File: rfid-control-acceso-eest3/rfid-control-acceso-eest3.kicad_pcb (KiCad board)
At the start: 2 copper layers, 120 x 80 mm, 71 parts, among them J1 BOARD_12VDC_2.5A, J10 PIR_TAMPER, J11 PIR_PWR, J12 PIR_ALARM, J13 ESP32-S3-DevKitC-1_N16R8_44P, J2 BUCK?, J5 RC522_8PIN_3V3_PINOUT_PENDING, J6 REED_NC, J8 CABINET_SENSOR, J9 LOCK_12V_1.8A_21.6W, Q1 AO3400A_PRELIM, Q2 AO3400A_PRELIM

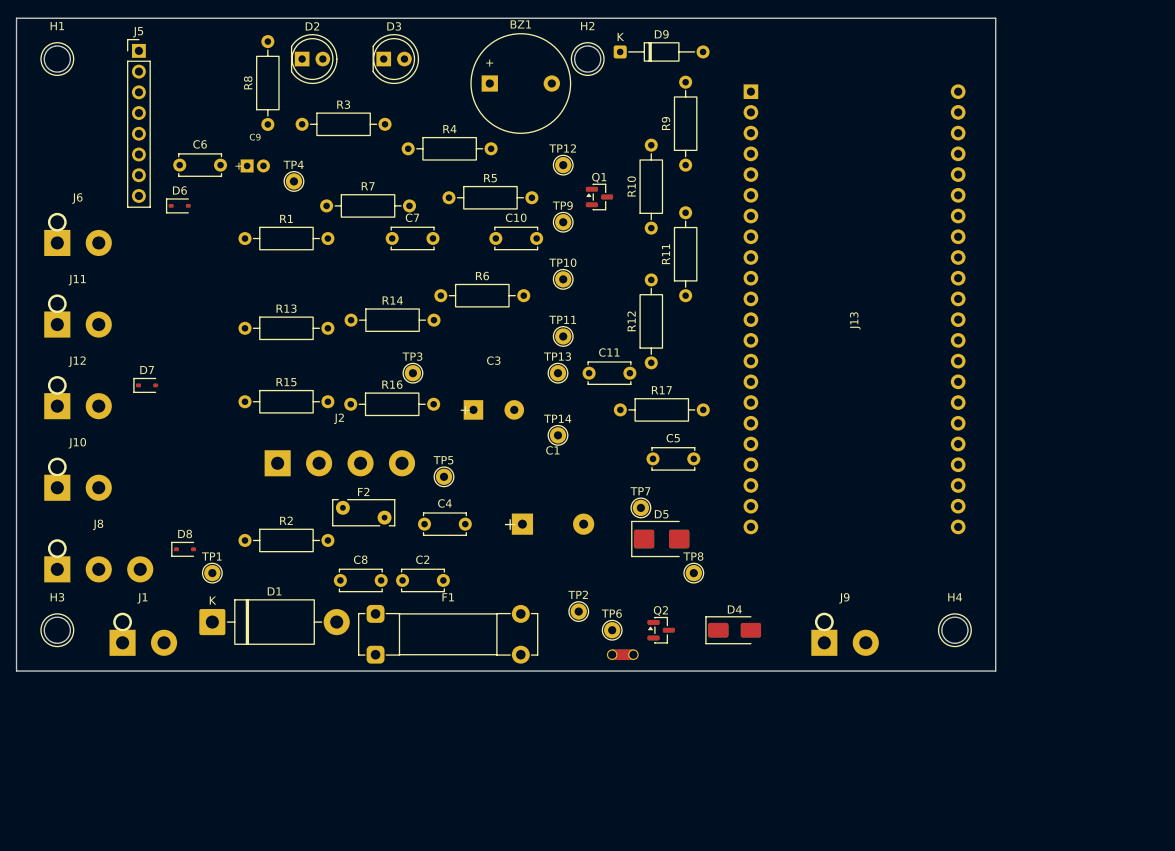
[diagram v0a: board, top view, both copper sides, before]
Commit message: Corrige tres diodos invertidos, netclasses y recalcula el floorplan
Errores electricos, verificados regenerando el netlist con kicad-cli:

- D1 tenia el catodo en +12V_IN y el anodo hacia F1, o sea bloqueaba la
  polaridad correcta. Montado asi la placa no encendia.
- D2 y D3 tenian el anodo a GND y el catodo hacia R3/R4. Como un GPIO nunca
  baja de 0 V, los LEDs no podian encender.
- La red entre D1 y F1 no coincidia con ningun patron de netclass y heredaba
  Default: 0,2 mm de pista para ~2,2 A. Pasa a LOCK_POWER (2,0 mm), igual que
  +12V_IN, que estaba en POWER_12V_AUX (0,8 mm).
- Al girar los LEDs, KiCad renombro las redes autogeneradas. Las netclasses
  apuntaban a los nombres viejos; se re-apuntaron.

Footprints: se eliminan los ocho PLACEHOLDER_NO_FABRICAR. Todos tenian
equivalente real ya instalado en KiCad 10. C9 pasa a MLCC 1206: tenia simbolo
no polarizado con footprint de electrolitico. El unico footprint local que
queda es el del ESP32-S3, con la hilera par duplicada en 22,86 y 25,40 mm
porque no se midio el modulo fisico. El paso doble cubre la separacion, no el
orden de pines: hay que verificar 3V3, EN, 5V y GND por continuidad antes de
soldar.

Floorplan: la posicion real de los pines de J13 determina el orden de los
bloques, y estaban casi invertidos. Lazo de potencia J1-J9 de 86 a 38 mm,
estrella de masa NT1-J1 de 60 a 9 mm, SPI de ~70 a 8,7 mm. Contorno de 120x80
a 140x100 mm: la densidad bajaba de 53% a 36% y la caja sigue sin definir.

Sigue sin ruteo, sin vias y sin archivos de fabricacion. Falta ejecutar
Update PCB from Schematic en la GUI: KiCad no expone esa operacion por CLI.

Co-Authored-By: Claude Opus 5 <noreply@anthropic.com>
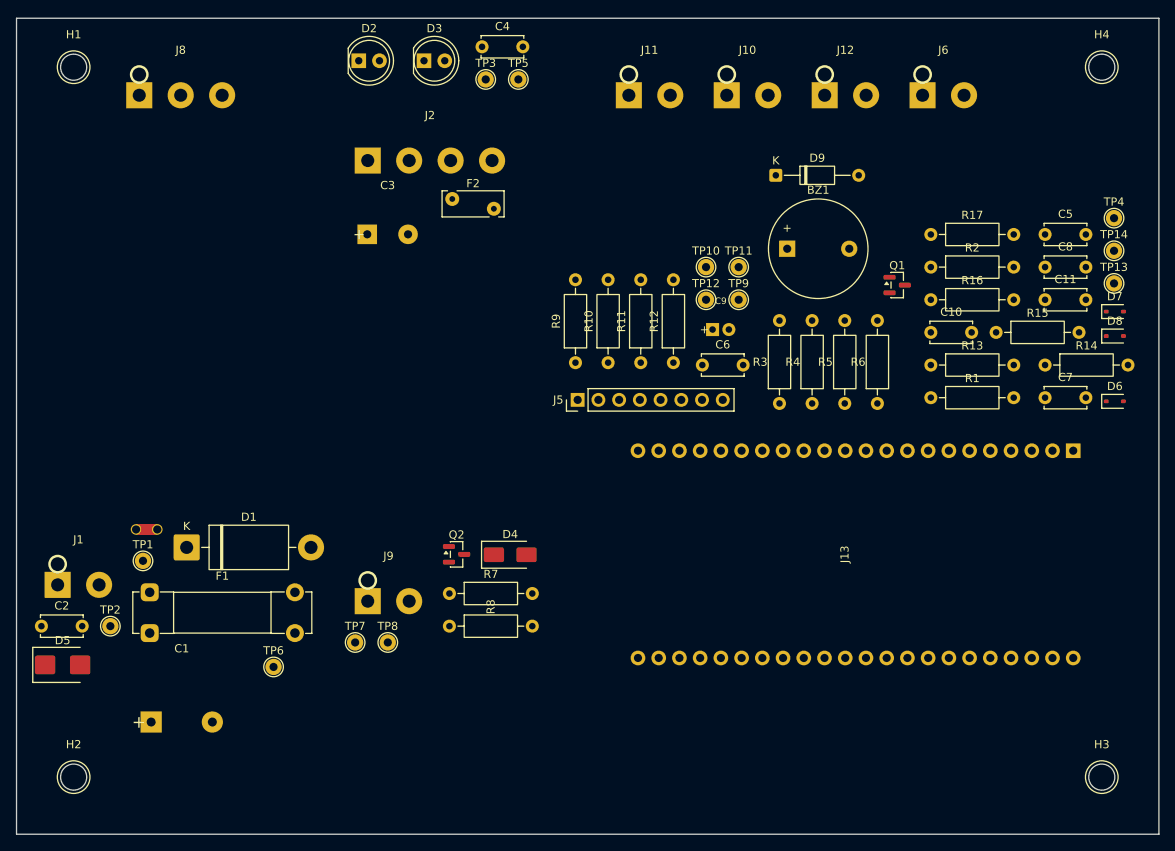
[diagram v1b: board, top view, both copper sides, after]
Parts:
- H1, H2, H3, H4: footprint rfid_eest3:MOUNTING_HOLE_3.2_PLACEHOLDER_NO_FABRICAR -> MountingHole:MountingHole_3.2mm_M3
- moved H3 129.3 mm to (153.0, 113.0)
- moved D7 118.9 mm to (154.6, 56.0)
- moved D6 117.1 mm to (154.6, 67.0)
- moved D8 116.9 mm to (154.6, 59.0)
- moved H2 108.2 mm to (27.0, 113.0)
- moved J6 107.6 mm to (131.0, 26.9)
- moved J12 101.5 mm to (119.0, 26.9)
- moved TP4 100.6 mm to (154.5, 44.5)
- moved J10 95.1 mm to (107.0, 26.9)
- moved C8 94.5 mm to (146.1, 50.5)
- moved R15 92.4 mm to (140.1, 58.5)
- moved R2 90.5 mm to (132.1, 50.5)
- moved R1 86.3 mm to (132.1, 66.5)
- moved R14 85.2 mm to (146.1, 62.5)
- moved R13 84.2 mm to (132.1, 62.5)
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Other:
- board size 120 x 80 mm -> 140 x 100 mm

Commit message: Lleva J5 al borde y le pone conector con traba para el lector del marco
El RC522 va montado en el marco de la puerta y se conecta por cable. J5 estaba
en el medio de la placa, asi que el cable tenia que cruzar por encima de todo
el board. Se mueve al borde superior, junto a las borneras de sensores: todos
los cables que van hacia la puerta salen por el mismo lado y el borde inferior
queda para potencia y cerradura.

El footprint pasa de PinHeader_1x08_P2.54mm_Vertical a JST_XH_S8B-XH-A
horizontal: con traba y entrada lateral. Un header con jumpers dupont falla de
forma intermitente en algo que golpea cada vez que se abre la puerta.

La traza SPI sube de 8,7 a 43,7 mm. Es irrelevante: con el reloj a 1 MHz y las
resistencias serie de 33 ohm, el factor dominante son los 20-40 cm de cable, no
44 mm de pista.

Como el board conserva el footprint viejo hasta que se sincronice, la
colocacion reserva la union de ambas cajas. Sin eso J5 pisaba a J2 y el DRC
reportaba cortocircuito +3V3/GND de forma transitoria.

Se documentan en el informe las condiciones de instalacion del lector:
longitud de cable, separacion del metal del marco y desacoplo local.

Co-Authored-By: Claude Opus 5 <noreply@anthropic.com>
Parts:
- moved J5 43.6 mm to (77.0, 24.8), turned to 0 degrees
- moved F2 21.3 mm to (59.4, 58.1)
- moved J2 16.1 mm to (61.0, 50.9)
- moved C3 11.2 mm to (61.0, 35.5)
- moved C4 10.0 mm to (67.0, 23.5)
- moved D2 10.0 mm to (51.9, 25.2)
- moved D3 10.0 mm to (59.9, 25.2)
- moved TP3 10.0 mm to (67.5, 27.5)
- moved TP5 10.0 mm to (71.5, 27.5)
- moved J10 9.00 mm to (116.0, 26.9)
- moved J11 9.00 mm to (104.0, 26.9)
- moved J6 9.00 mm to (140.0, 26.9)
- moved J12 9.00 mm to (128.0, 26.9)
- moved R10 5.00 mm to (92.5, 67.2)
- moved R11 5.00 mm to (96.5, 67.2)
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
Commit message: Transfiere al board los footprints reales desde el esquema
Resultado de Update PCB from Schematic en la GUI, que kicad-cli no expone.

El board pasa a tener la geometria real: J13 con los 66 pads del footprint de
doble paso (el pad 2 existe en x=22,86 y en x=25,40), J5 como JST-XH de 8 vias,
C9 como 1206 y las ocho borneras como TerminalBlock_RND. Con esto los diodos
D1, D2 y D3 quedan por fin conectados segun el esquema corregido.

DRC: 28 infracciones, todas silk_overlap. Cero de biblioteca, cero de
courtyard, cero cortocircuitos. 122 pads sin conectar, que es lo esperado
porque no hay ninguna pista.

Co-Authored-By: Claude Opus 5 <noreply@anthropic.com>
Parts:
- C1: footprint rfid_eest3:CP_Radial_D16_P7.50_PLACEHOLDER_NO_FABRICAR -> Capacitor_THT:CP_Radial_D16.0mm_P7.50mm
- C3: footprint rfid_eest3:CP_Radial_D10_P5.00_PLACEHOLDER_NO_FABRICAR -> Capacitor_THT:CP_Radial_D10.0mm_P5.00mm_P7.50mm
- C9: value 10uF_PRELIMINAR -> 10uF_X5R_16V_1206; footprint rfid_eest3:CP_Radial_D5_P2.00_PLACEHOLDER_NO_FABRICAR -> Capacitor_SMD:C_1206_3216Metric
- J1, J10, J11, J12, J6, J9: footprint rfid_eest3:KF301_2P_P5.08_PLACEHOLDER_NO_FABRICAR -> TerminalBlock_RND:TerminalBlock_RND_205-00232_1x02_P5.08mm_Horizontal
- J13: footprint rfid_eest3:ESP32-S3-DevKitC-1-44P_PLACEHOLDER_NO_FABRICAR -> rfid_eest3:ESP32-S3-44P_SOCKET_DUAL_22.86_25.40
- J2: footprint rfid_eest3:KF301_4P_P5.08_PLACEHOLDER_NO_FABRICAR -> TerminalBlock_RND:TerminalBlock_RND_205-00234_1x04_P5.08mm_Horizontal
- J5: value RC522_8PIN_3V3_PINOUT_PENDING -> RC522_8PIN_3V3_XH_CABLE_LECTOR; footprint Connector_PinHeader_2.54mm:PinHeader_1x08_P2.54mm_Vertical -> Connector_JST:JST_XH_S8B-XH-A_1x08_P2.50mm_Horizontal
- J8: footprint rfid_eest3:KF301_3P_P5.08_PLACEHOLDER_NO_FABRICAR -> TerminalBlock_RND:TerminalBlock_RND_205-00233_1x03_P5.08mm_Horizontal
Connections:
- D1 pad 1: +12V_IN -> Net-(D1-K)
- D1 pad 2: Net-(D1-A) -> +12V_IN
- D2 pad 1: Net-(D2-K) -> GND
- D2 pad 2: GND -> Net-(D2-A)
- D3 pad 1: Net-(D3-K) -> GND
- D3 pad 2: GND -> Net-(D3-A)
- F1 pad 1: Net-(D1-A) -> Net-(D1-K)
- R3 pad 2: Net-(D2-K) -> Net-(D2-A)
- R4 pad 2: Net-(D3-K) -> Net-(D3-A)

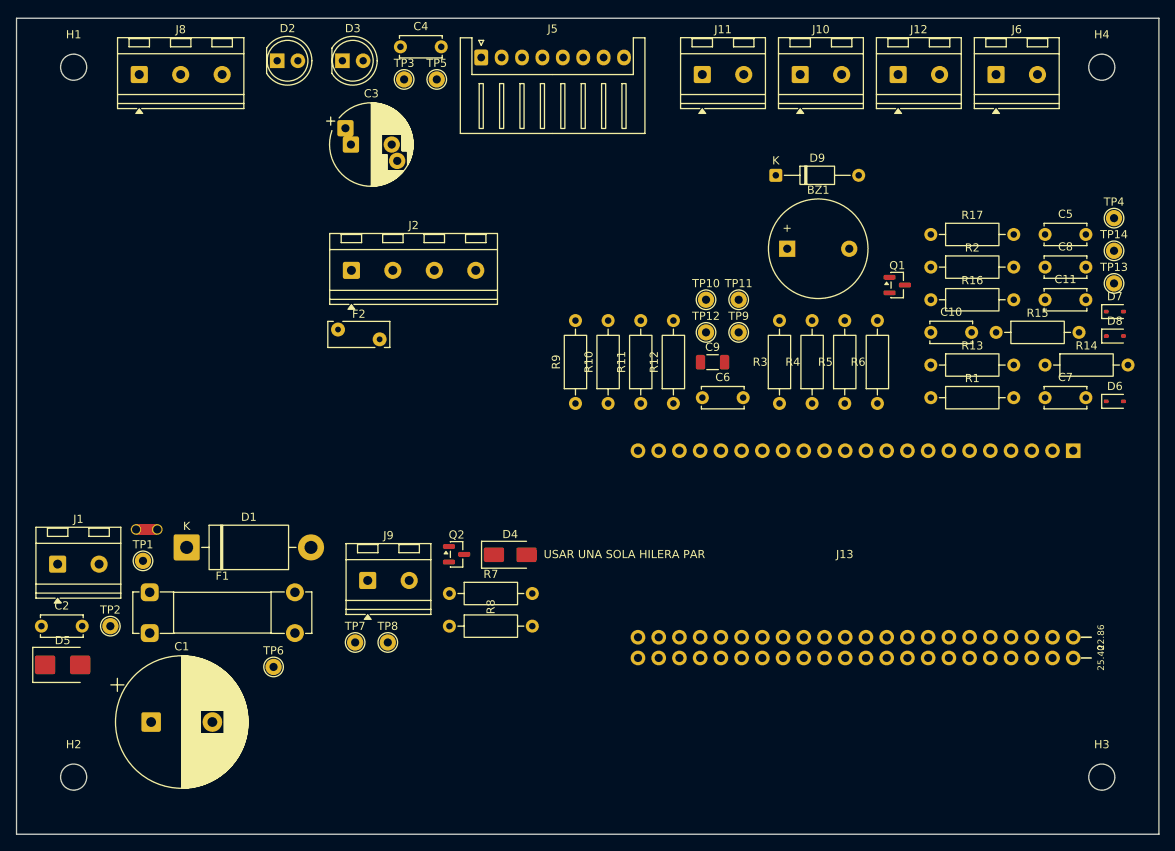
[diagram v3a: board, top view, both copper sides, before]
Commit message: Rutea la placa completa y ensancha las clases de red
349 pistas, 8 vias y 4 zonas, sin infracciones de margen ni de cobre. Quedan
3 no conectados: los pines 1 y 2 de J13, que caen dentro de las areas de
regla de la antena del modulo y no se pueden alcanzar con cobre. Los rieles
llegan por el pin 3 y por 42/43/44.

El ruteo va en tres pasos, y el orden importa (tools/):

1. preruteo_critico.py rutea a mano y bloquea las dos conexiones que ningun
   autorouter puede hacer: la fuente de Q2 al plano GND_POWER (la clase pide
   2 mm y el pad del SOT-23 mide 0,6) y el +3V3 del pin 3 de J13, que solo
   sale por debajo del modulo rodeando el extremo oeste.
2. autorutear.py hace el ida y vuelta con Freerouting por CLI, sin GUI.
3. planos_masa.py vierte los dos planos al final. Si estan puestos antes de
   autorutear, las señales cruzan B.Cu, parten el plano en islas y dejan 11
   pads de masa colgados.

Anchos: señal 0,25 -> 0,40 mm, alimentacion logica 0,50 -> 0,80 mm,
+12V_AUX 0,80 -> 1,00 mm, potencia 2,00 mm sin cambios. No queda ningun
tramo por debajo de 0,40 mm salvo 2,7 mm de transiciones en los pads de Q2.

GND_POWER y GND se tocan unicamente en NT1: son redes distintas y el net-tie
es el unico puente posible. El plano de potencia queda entero en una sola
isla.

Pendiente, y es emplazamiento y no ruteo: D4 esta a 15 mm de J9, y eso deja
el lazo de recirculacion de la cerradura en unos 30 mm de perimetro.

Co-Authored-By: Claude Opus 5 <noreply@anthropic.com>
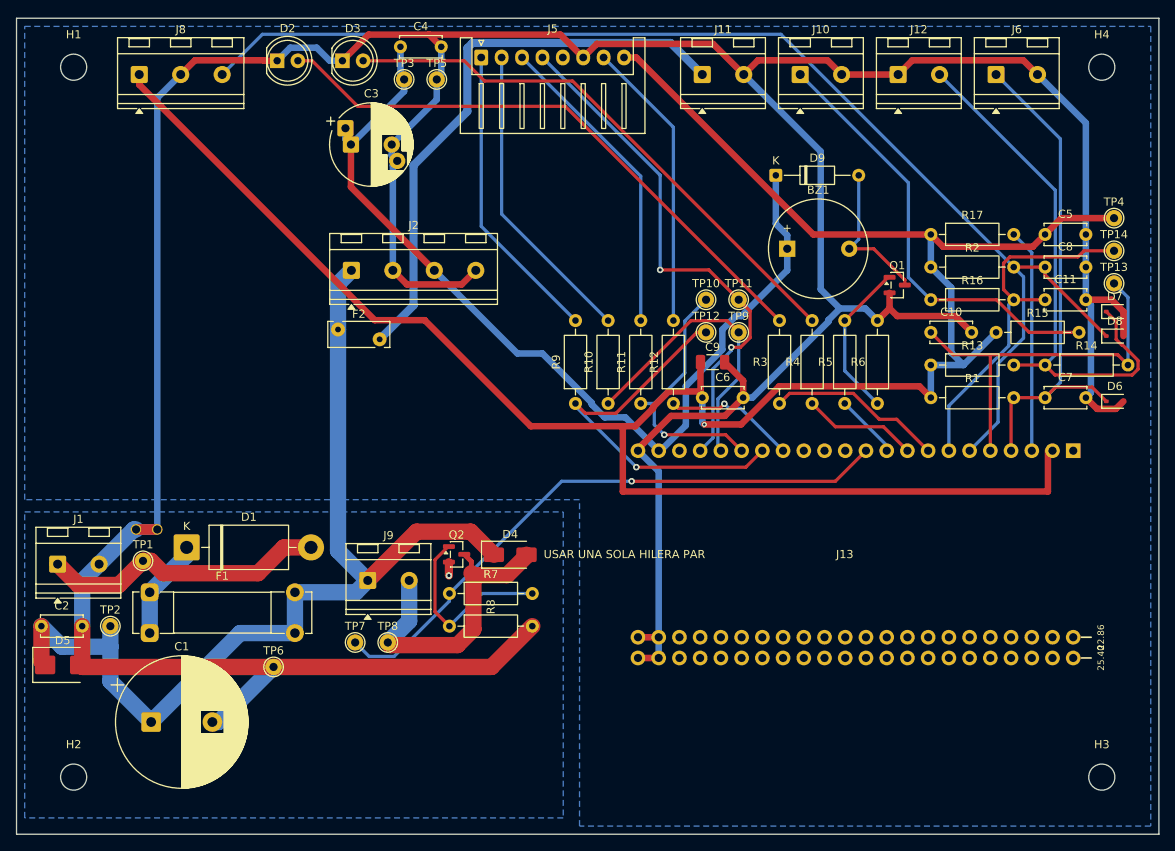
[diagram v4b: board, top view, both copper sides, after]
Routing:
- net GND: track 0.00 -> 395.2 mm
- net +3V3: track 0.00 -> 294.8 mm, vias 0 -> 1
- net CABINET_SENSOR: track 0.00 -> 152.0 mm
- net +12V_LOCK: track 0.00 -> 124.2 mm
- net +5V: track 0.00 -> 115.0 mm
- net GND_POWER: track 0.00 -> 89.1 mm, vias 0 -> 1
- net LOCK_GATE: track 0.00 -> 74.3 mm, vias 0 -> 1
- net Net-(D2-A): track 0.00 -> 72.2 mm
- net +12V_AUX: track 0.00 -> 70.8 mm
- net Net-(D3-A): track 0.00 -> 68.2 mm
- net /4_SENSORES/PIR_CONTACT: track 0.00 -> 66.8 mm
- net RFID_MISO: track 0.00 -> 65.4 mm, vias 0 -> 2
- net DOOR_REED: track 0.00 -> 62.9 mm
- net /4_SENSORES/PIR_TAMPER_CONTACT: track 0.00 -> 54.0 mm
- net PIR_IN: track 0.00 -> 48.3 mm
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- added copper zone on B.Cu, net GND
- added copper zone on B.Cu, net GND_POWER
